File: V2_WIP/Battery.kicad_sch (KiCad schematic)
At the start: 21 parts, among them J601 BATT, SW602 MSN22AFW01, U601 *IP5306, U602 STC3100IST

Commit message: updated list of changes in README.md
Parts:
- added D1: Zener, Diode_SMD:D_SOD-523, symbol Device:D_Zener_Small
- added R105: 1k, Resistor_SMD:R_0603_1608Metric_Pad0.98x0.95mm_HandSolder, symbol Device:R
- added R107: 150, Resistor_SMD:R_0603_1608Metric_Pad0.98x0.95mm_HandSolder, symbol Device:R
- added TP4: KEY, TestPoint:TestPoint_Pad_D1.0mm, symbol Connector:TestPoint
- TP601, TP602: footprint TestPoint:TestPoint_Pad_D1.5mm -> TestPoint:TestPoint_Pad_D1.0mm
- U602: footprint Package_SO:SO-8_3.9x4.9mm_P1.27mm -> Package_SON:WSON-8-1EP_8x6mm_P1.27mm_EP3.4x4.3mm; DESCRIPTION STC3100 Series 5.5 V Battery Monitor IC with Coulomb Counte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 -> (none); PACKAGE TSSOP-8 STMicroelectronics -> (none); PRICE None -> (none)
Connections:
- net +5V: no longer C608.1, U602.7 (VCC)
- net BATT: no longer C609.1, U602.8 (VIN)
- net GND: now also D1.2 (A)
- net at J601.1 (Pin_1), SW602.2 (B): now also R105.2, R107.1
- net at R_E601.1, U601.5 (KEY): now also TP4.1
- new net: C609.1, R105.1, U602.8 (VIN)
- new net: C608.1, D1.1 (K), R107.2, U602.7 (VCC)
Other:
- note added: "- +"
- note added: "Rcg <= 0.08/peak_current_A 33mOhm => peak +/-2A"
- moved on the sheet: C601, C602, C603, C604, C605, C606, C609, C610, L601, R_E601, R_E602, R_E603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

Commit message: changed footprints of U102 and U602
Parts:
- U602: footprint Package_SON:WSON-8-1EP_8x6mm_P1.27mm_EP3.4x4.3mm -> KiCad:SOIC65P490X110-8N
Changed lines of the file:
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@@
 	(text "Battery connection"
 		(exclude_from_sim no)
-		(at 251.46 64.77 0)
+		(at 261.366 20.066 0)
 		(effects
 			(font
@@
 			)
 		)
-		(property "Footprint" "Package_SON:WSON-8-1EP_8x6mm_P1.27mm_EP3.4x4.3mm"
+		(property "Footprint" "KiCad:SOIC65P490X110-8N"
 			(at 190.5 113.03 0)
 			(hide yes)

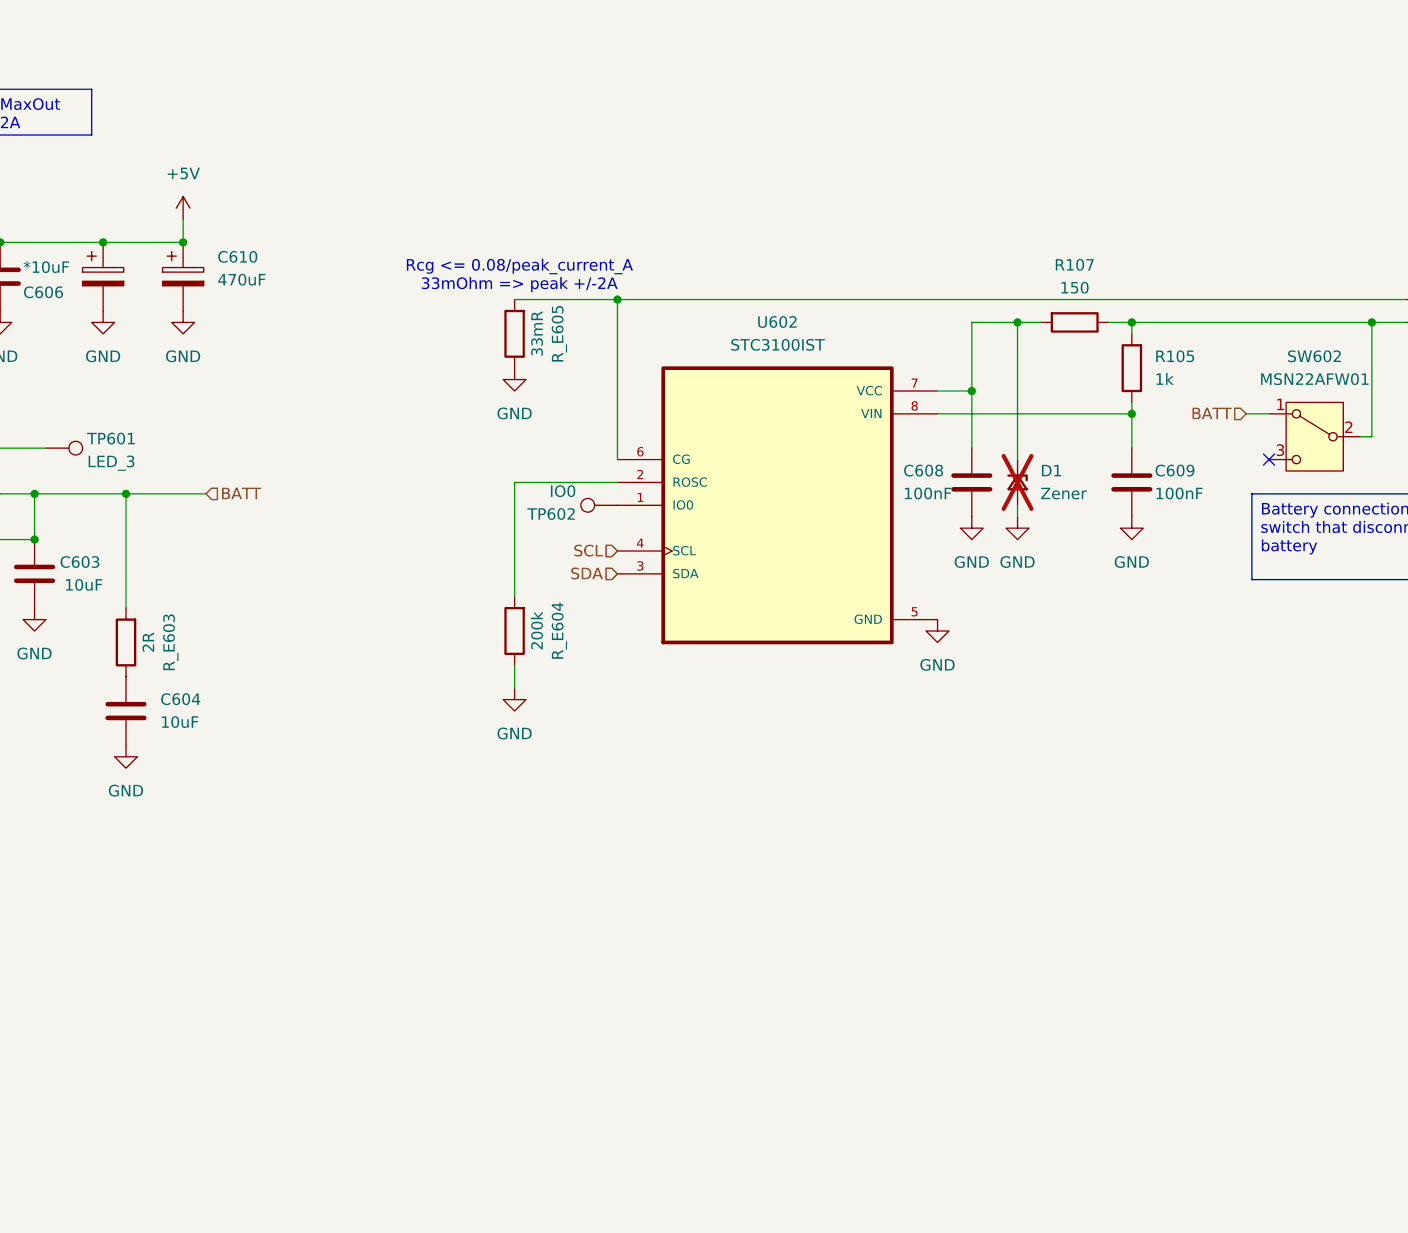
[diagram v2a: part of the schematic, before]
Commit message: reworked the schematic, changed differential pairs and RF traces, small PCB adjustments
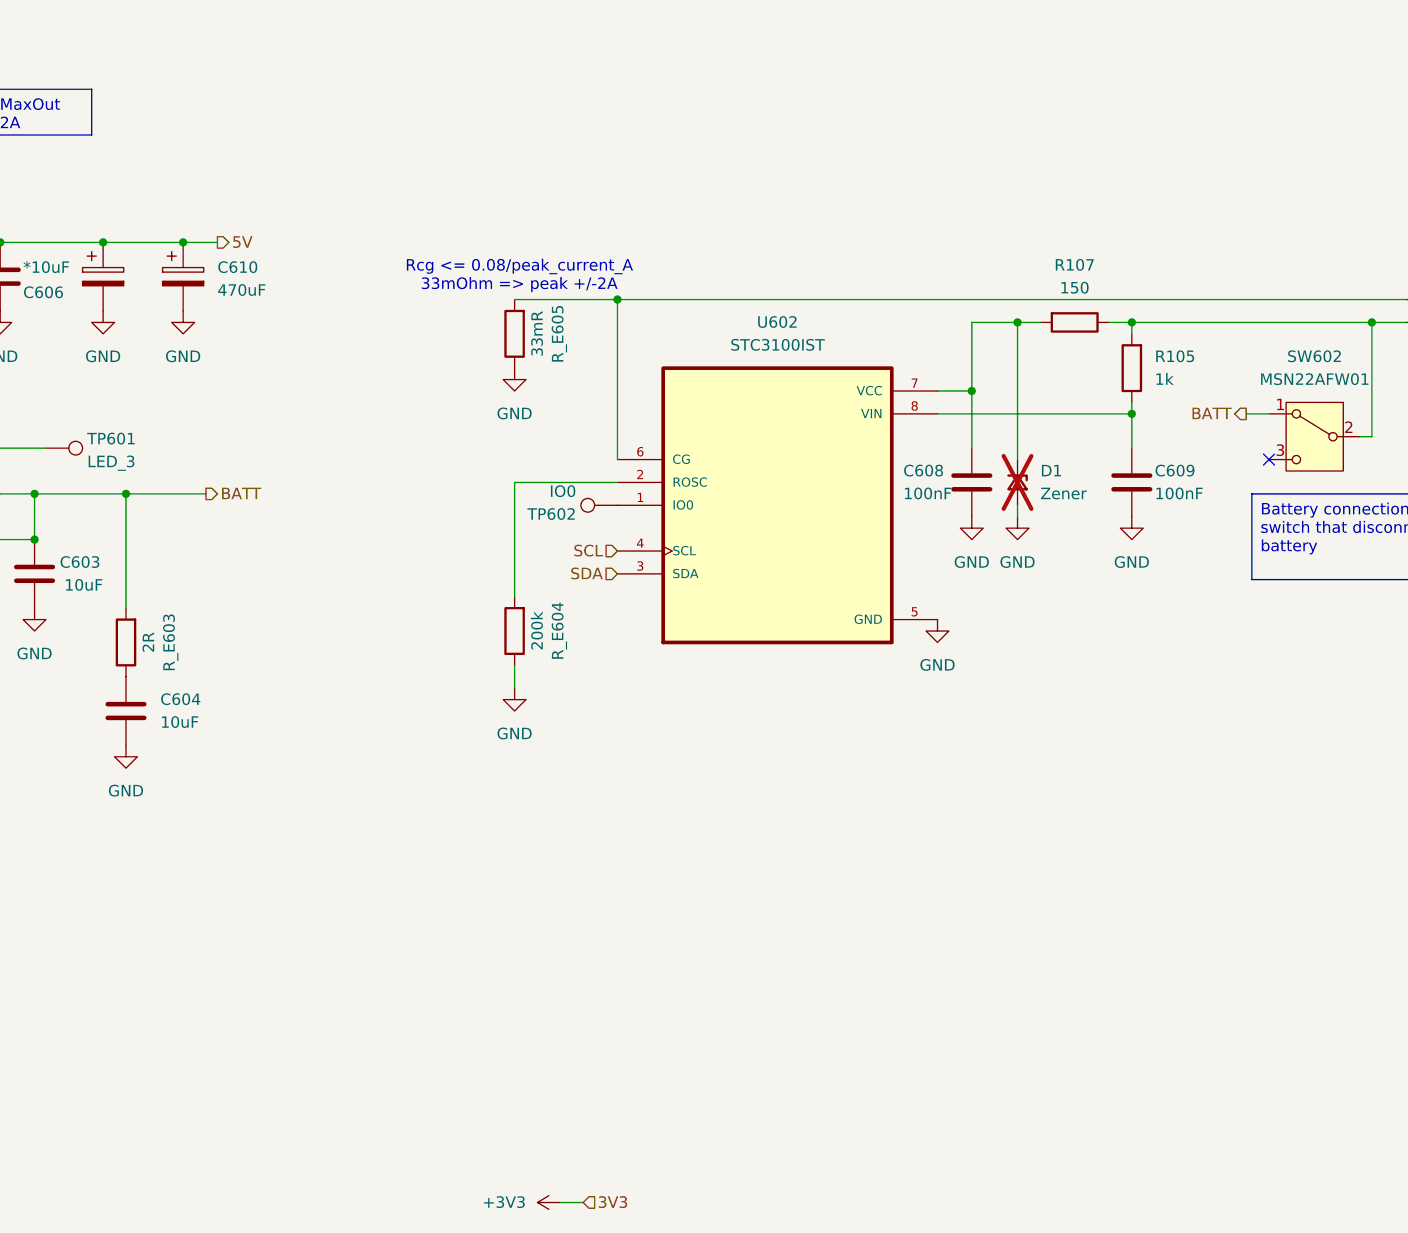
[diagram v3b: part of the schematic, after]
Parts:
- C606: footprint Capacitor_Tantalum_SMD:CP_EIA-3528-15_AVX-H_Pad1.50x2.35mm_HandSolder -> Capacitor_Tantalum_SMD:CP_EIA-3528-21_Kemet-B_HandSolder
- SW602: footprint Button_Switch_THT:MSN22AFW01 -> KiCad:MSN22AFW01
- U601: footprint Package_SO:SOP-8L -> KiCad:SOP127P600X165-9N
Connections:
- net +5V renamed 5V
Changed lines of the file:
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@@
 	)
 	(junction
-		(at 30.48 101.6)
+		(at 124.46 83.82)
 		(diameter 0)
 		(color 0 0 0 0)
 	)
 	(junction
-		(at 44.45 96.52)
+		(at 115.57 83.82)
 		(diameter 0)
 		(color 0 0 0 0)
 	)
 	(junction
-		(at 115.57 83.82)
+		(at 30.48 101.6)
 		(diameter 0)
 		(color 0 0 0 0)
 	)
 	(junction
-		(at 229.87 92.71)
+		(at 44.45 96.52)
 		(diameter 0)
 		(color 0 0 0 0)
 	)
 	(junction
-		(at 107.95 116.84)
+		(at 229.87 92.71)
 		(diameter 0)
 		(color 0 0 0 0)
 	)
 	(junction
-		(at 107.95 111.76)
+		(at 107.95 116.84)
 		(diameter 0)
 		(color 0 0 0 0)
 	)
 	(junction
-		(at 124.46 83.82)
+		(at 107.95 111.76)
 		(diameter 0)
 		(color 0 0 0 0)
@@
 	(wire
 		(pts
-			(xy 124.46 81.28) (xy 124.46 83.82)
+			(xy 212.09 92.71) (xy 217.17 92.71)
 		)
 		(stroke
@@
 	(wire
 		(pts
-			(xy 212.09 92.71) (xy 217.17 92.71)
+			(xy 212.09 92.71) (xy 212.09 100.33)
 		)
 		(stroke
@@
 	(wire
 		(pts
-			(xy 212.09 92.71) (xy 212.09 100.33)
+			(xy 128.27 83.82) (xy 124.46 83.82)
 		)
 		(stroke
@@
 	(wire
 		(pts
+			(xy 166.37 190.5) (xy 168.91 190.5)
+		)
+		(stroke
+			(width 0)
+			(type default)
+		)
+	)
+	(wire
+		(pts
 			(xy 172.72 90.17) (xy 260.35 90.17)
 		)
@@
 	)
 	(hierarchical_label "BATT"
-		(shape input)
+		(shape output)
 		(at 242.57 102.87 180)
 		(effects
@@
 		)
 	)
+	(hierarchical_label "5V"
+		(shape output)
+		(at 128.27 83.82 0)
+		(effects
+			(font
+				(size 1.27 1.27)
+			)
+			(justify left)
+		)
+	)
 	(hierarchical_label "BATT"
-		(shape input)
+		(shape output)
 		(at 127 111.76 0)
 		(effects
@@
 		)
 	)
+	(hierarchical_label "3V3"
+		(shape input)
+		(at 168.91 190.5 0)
+		(effects
+			(font
+				(size 1.27 1.27)
+			)
+			(justify left)
+		)
+	)
 	(symbol
 		(lib_id "Device:R")
@@
 			)
 		)
-		(property "Footprint" "Button_Switch_THT:MSN22AFW01"
+		(property "Footprint" "KiCad:MSN22AFW01"
 			(at 250.19 105.41 0)
 			(hide yes)
@@
 	)
 	(symbol
-		(lib_id "power:+5V")
-		(at 124.46 81.28 0)
-		(unit 1)
-		(body_style 1)
-		(exclude_from_sim no)
-		(in_bom yes)
-		(on_board yes)
-		(in_pos_files yes)
-		(dnp no)
-		(fields_autoplaced yes)
-		(property "Reference" "#PWR0601"
-			(at 124.46 85.09 0)
-			(hide yes)
-			(show_name no)
-			(do_not_autoplace no)
-			(effects
-				(font
-					(size 1.27 1.27)
-				)
-			)
-		)
-		(property "Value" "+5V"
-			(at 124.46 76.2 0)
-			(show_name no)
-			(do_not_autoplace no)
-			(effects
-				(font
-					(size 1.27 1.27)
-				)
-			)
-		)
-		(property "Footprint" ""
-			(at 124.46 81.28 0)
-			(hide yes)
-			(show_name no)
-			(do_not_autoplace no)
-			(effects
-				(font
-					(size 1.27 1.27)
-				)
-			)
-		)
-		(property "Datasheet" ""
-			(at 124.46 81.28 0)
-			(hide yes)
-			(show_name no)
-			(do_not_autoplace no)
-			(effects
-				(font
-					(size 1.27 1.27)
-				)
-			)
-		)
-		(property "Description" "Power symbol creates a global label with name \"+5V\""
-			(at 124.46 81.28 0)
-			(hide yes)
-			(show_name no)
-			(do_not_autoplace no)
-			(effects
-				(font
-					(size 1.27 1.27)
-				)
-			)
-		)
-		(pin "1"
-		)
-		(instances
-			(project "gps"
-				(path "/00526ddc-5304-4072-af1e-192a9e7e83da/280f742a-a734-4c07-ab96-9dbf73329b01"
-					(reference "#PWR0601")
-					(unit 1)
-				)
-			)
-		)
-	)
-	(symbol
 		(lib_id "power:GND")
 		(at 212.09 114.3 0)
@@
 			)
 		)
-		(property "Footprint" "Package_SO:SOP-8L"
+		(property "Footprint" "KiCad:SOP127P600X165-9N"
 			(at 78.74 109.22 0)
 			(hide yes)
@@
 			)
 		)
-		(property "Footprint" "Capacitor_Tantalum_SMD:CP_EIA-3528-15_AVX-H_Pad1.50x2.35mm_HandSolder"
+		(property "Footprint" "Capacitor_Tantalum_SMD:CP_EIA-3528-21_Kemet-B_HandSolder"
 			(at 116.5352 91.44 0)
 			(hide yes)
@@
 	)
 	(symbol
+		(lib_id "power:+3V3")
+		(at 166.37 190.5 90)
+		(unit 1)
+		(body_style 1)
+		(exclude_from_sim no)
+		(in_bom yes)
+		(on_board yes)
+		(in_pos_files yes)
+		(dnp no)
+		(fields_autoplaced yes)
+		(property "Reference" "#PWR0427"
+			(at 170.18 190.5 0)
+			(hide yes)
+			(show_name no)
+			(do_not_autoplace no)
+			(effects
+				(font
+					(size 1.27 1.27)
+				)
+			)
+		)
+		(property "Value" "+3V3"
+			(at 162.56 190.4999 90)
+			(show_name no)
+			(do_not_autoplace no)
+			(effects
+				(font
+					(size 1.27 1.27)
+				)
+				(justify left)
+			)
+		)
+		(property "Footprint" ""
+			(at 166.37 190.5 0)
+			(hide yes)
+			(show_name no)
+			(do_not_autoplace no)
+			(effects
+				(font
+					(size 1.27 1.27)
+				)
+			)
+		)
+		(property "Datasheet" ""
+			(at 166.37 190.5 0)
+			(hide yes)
+			(show_name no)
+			(do_not_autoplace no)
+			(effects
+				(font
+					(size 1.27 1.27)
+				)
+			)
+		)
+		(property "Description" "Power symbol creates a global label with name \"+3V3\""
+			(at 166.37 190.5 0)
+			(hide yes)
+			(show_name no)
+			(do_not_autoplace no)
+			(effects
+				(font
+					(size 1.27 1.27)
+				)
+			)
+		)
+		(pin "1"
+		)
+		(instances
+			(project "gps"
+				(path "/00526ddc-5304-4072-af1e-192a9e7e83da/280f742a-a734-4c07-ab96-9dbf73329b01"
+					(reference "#PWR0427")
+					(unit 1)
+				)
+			)
+		)
+	)
+	(symbol
 		(lib_id "Device:C_Polarized")
 		(at 124.46 87.63 0)
@@
 		(in_pos_files yes)
 		(dnp no)
-		(fields_autoplaced yes)
 		(property "Reference" "C610"
-			(at 128.27 85.4709 0)
+			(at 128.27 86.614 0)
 			(show_name no)
 			(do_not_autoplace no)
@@
 		)
 		(property "Value" "470uF"
-			(at 128.27 88.0109 0)
+			(at 128.27 89.154 0)
 			(show_name no)
 			(do_not_autoplace no)

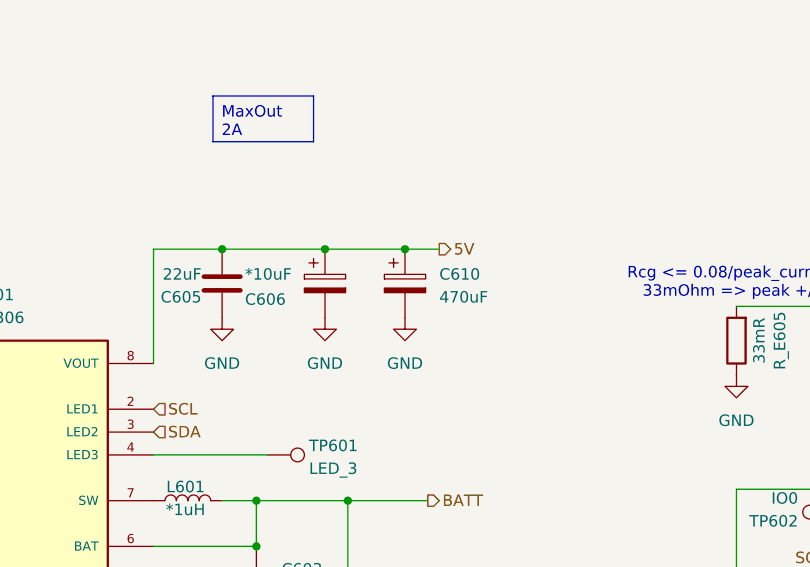
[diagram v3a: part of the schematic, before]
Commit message: adjusted elec capacitors
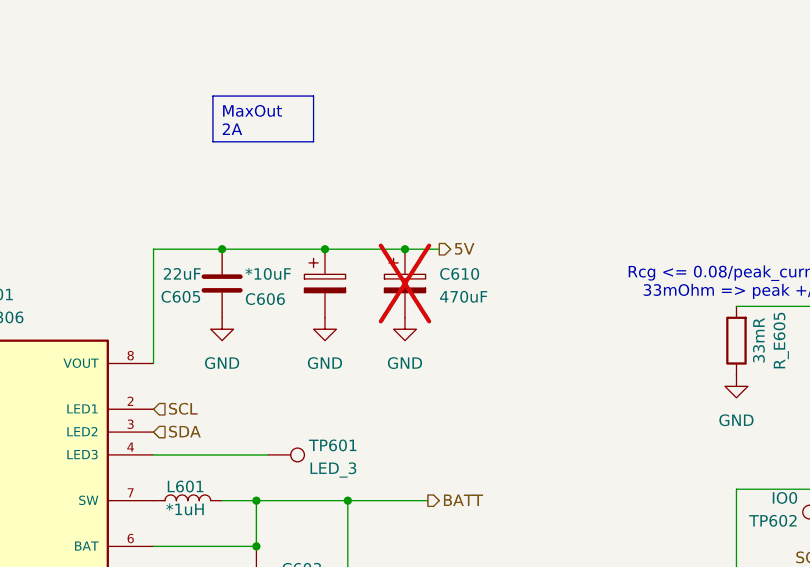
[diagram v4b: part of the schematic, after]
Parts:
- C610: now not fitted
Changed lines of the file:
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@@
 		(on_board yes)
 		(in_pos_files yes)
-		(dnp no)
+		(dnp yes)
 		(property "Reference" "C610"
 			(at 128.27 86.614 0)
